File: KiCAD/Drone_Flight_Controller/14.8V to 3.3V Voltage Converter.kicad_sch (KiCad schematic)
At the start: 14 parts, among them Q1 BUJ303B,127, U4 AS358, U6 AS358

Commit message: Fix Bugs
Fix Bugs
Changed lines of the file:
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@@
-	)
-	(junction
-		(at 189.23 101.6)
-		(diameter 0)
-		(color 0 0 0 0)
 	)
 	(junction
@@
 	(wire
 		(pts
-			(xy 196.85 101.6) (xy 189.23 101.6)
-		)
-		(stroke
-			(width 0)
-			(type default)
-		)
-	)
-	(wire
-		(pts
 			(xy 162.56 90.17) (xy 165.1 90.17)
 		)
@@
 	(wire
 		(pts
-			(xy 114.3 111.76) (xy 87.63 111.76)
+			(xy 124.46 111.76) (xy 87.63 111.76)
 		)
 		(stroke
@@
 	(wire
 		(pts
-			(xy 114.3 90.17) (xy 114.3 111.76)
+			(xy 124.46 90.17) (xy 124.46 111.76)
 		)
 		(stroke
@@
 	(wire
 		(pts
-			(xy 196.85 99.06) (xy 196.85 101.6)
-		)
-		(stroke
-			(width 0)
-			(type default)
-		)
-	)
-	(wire
-		(pts
 			(xy 87.63 111.76) (xy 87.63 90.17)
 		)
@@
 	(wire
 		(pts
-			(xy 114.3 90.17) (xy 127 90.17)
+			(xy 124.46 90.17) (xy 127 90.17)
 		)
 		(stroke
@@
 			)
 		)
-		(property "Datasheet" "https://www.mouser.at/datasheet/2/115/DIOD_S_A0005046231_1-2542568.pdf"
+		(property "Datasheet" "~"
 			(at 154.94 90.17 0)
 			(effects
@@
 					(unit 1)
 				)
-			)
-		)
-	)
-	(symbol
-		(lib_id "power:PWR_FLAG")
-		(at 196.85 99.06 0)
-		(unit 1)
-		(exclude_from_sim no)
-		(in_bom yes)
-		(on_board yes)
-		(dnp no)
-		(fields_autoplaced yes)
-		(property "Reference" "#FLG01"
-			(at 196.85 97.155 0)
-			(effects
-				(font
-					(size 1.27 1.27)
-				)
-				(hide yes)
-			)
-		)
-		(property "Value" "PWR_FLAG"
-			(at 196.85 93.98 0)
-			(effects
-				(font
-					(size 1.27 1.27)
-				)
-			)
-		)
-		(property "Footprint" ""
-			(at 196.85 99.06 0)
-			(effects
-				(font
-					(size 1.27 1.27)
-				)
-				(hide yes)
-			)
-		)
-		(property "Datasheet" "~"
-			(at 196.85 99.06 0)
-			(effects
-				(font
-					(size 1.27 1.27)
-				)
-				(hide yes)
-			)
-		)
-		(property "Description" "Special symbol for telling ERC where power comes from"
-			(at 196.85 99.06 0)
-			(effects
-				(font
-					(size 1.27 1.27)
-				)
-				(hide yes)
-			)
-		)
-		(pin "1"
-		)
-		(instances
-			(project ""
-				(path "/05daaa24-e506-4b9a-9564-8bf799413ca8/93fa31b3-ffc2-4fc8-af5e-8c3024b36dbd"
-					(reference "#FLG01")
-					(unit 1)
-				)

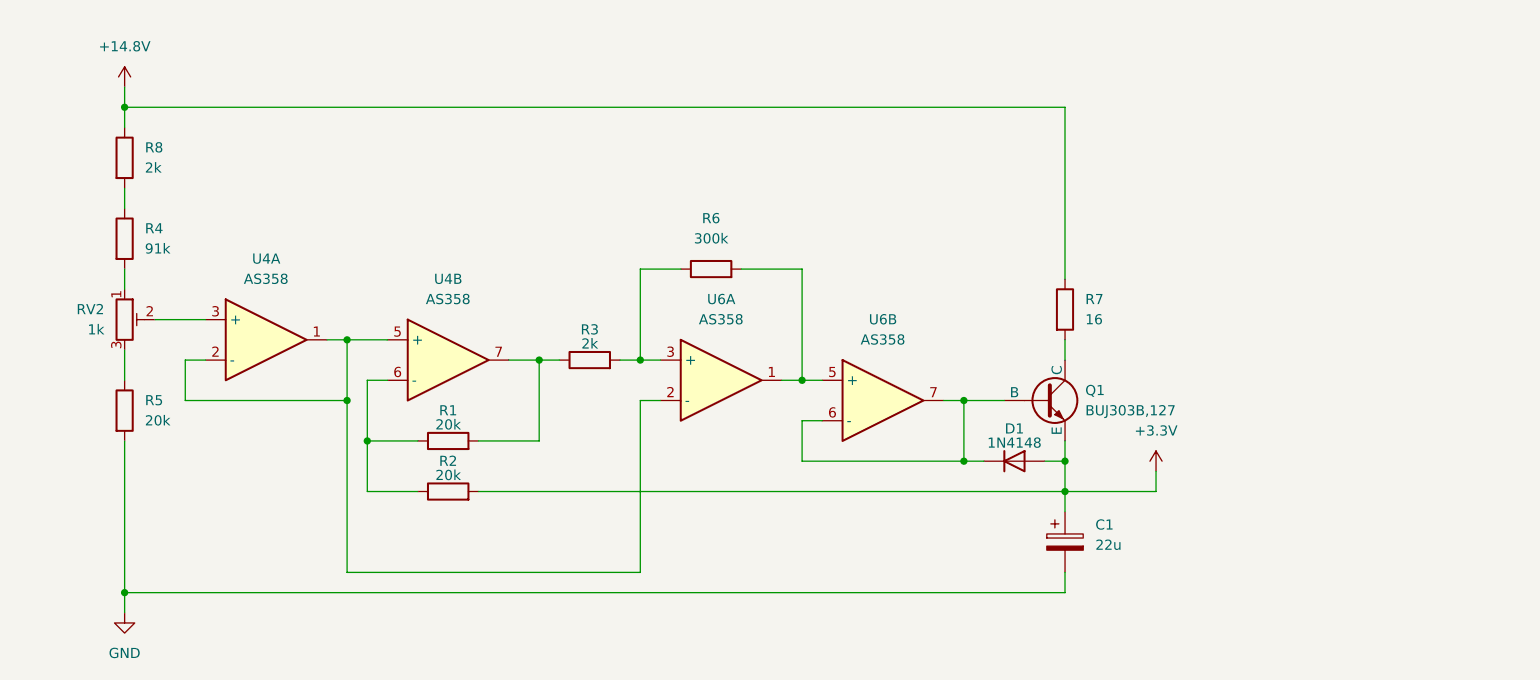
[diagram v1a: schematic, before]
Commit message: Change +14.8V & GND to +BATT & -BATT
Change +14.8V& GND to +BATT & -BATT
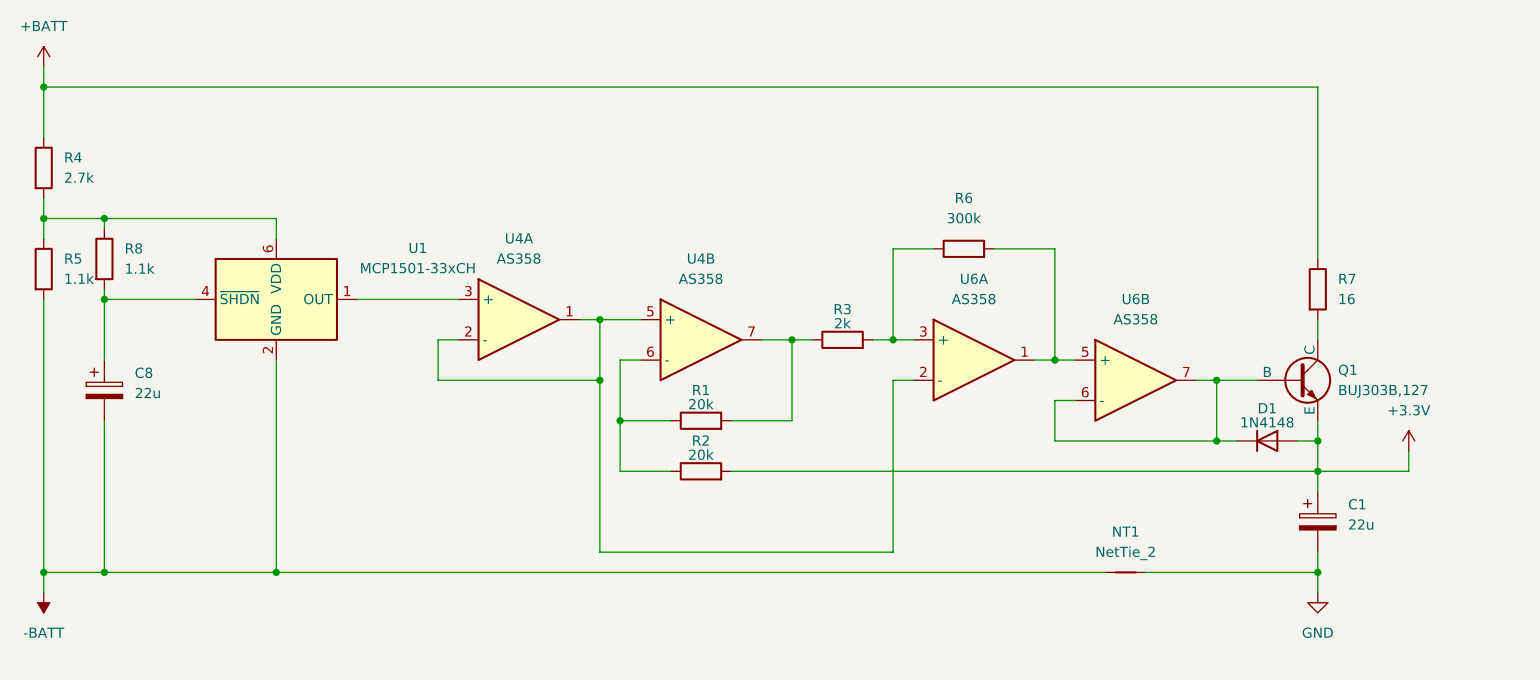
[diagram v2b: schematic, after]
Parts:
- removed RV2: 1k, Potentiometer_SMD:Potentiometer_Bourns_3214X_Vertical, symbol Device:R_Potentiometer_Trim
- added C8: 22u, Capacitor_THT:CP_Radial_D5.0mm_P2.00mm, symbol Device:C_Polarized
- added NT1: NetTie_2, symbol Device:NetTie_2
- added U1: MCP1501-33xCH, Package_TO_SOT_SMD:SOT-23-6, symbol Reference_Voltage:MCP1501-33xCH
- R4: value 91k -> 2.7k; footprint Resistor_SMD:R_0805_2012Metric_Pad1.20x1.40mm_HandSolder -> (none); Link https://www.mouser.at/ProductDetail/KOA-Speer/RN73R2ATTD750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 -> (none)
- R5: value 20k -> 1.1k; footprint Resistor_SMD:R_0805_2012Metric_Pad1.20x1.40mm_HandSolder -> (none); Link https://www.mouser.at/ProductDetail/Panasonic/ERA-6AEB203V?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 -> (none)
- R8: value 2k -> 1.1k; footprint Resistor_SMD:R_0805_2012Metric_Pad1.20x1.40mm_HandSolder -> (none); Link https://www.mouser.at/ProductDetail/YAGEO/RT0805BRD072KL?qs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 -> (none)
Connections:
- net GND: now also NT1.2; no longer R5.2
- net at R4.2: now also R5.1, R8.1, U1.6 (VDD)
- net at U4.3 (+): now also U1.1 (OUT)
- net at R8.2: now also C8.1, U1.4 (~{SHDN}); no longer R4.1
- net +14.8V renamed +BATT
- net +BATT: now also R4.1; no longer R8.1
- new net -BATT: C8.2, NT1.1, R5.2, U1.2 (GND), U1.3 (GND), U1.5 (GND)
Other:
- moved on the sheet: C1, D1, Q1, R1, R2, R3, R6, R7, U4A, U4B, U6A, U6B

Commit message: Add USB & Status LEDS
Add USB & Status LEDS
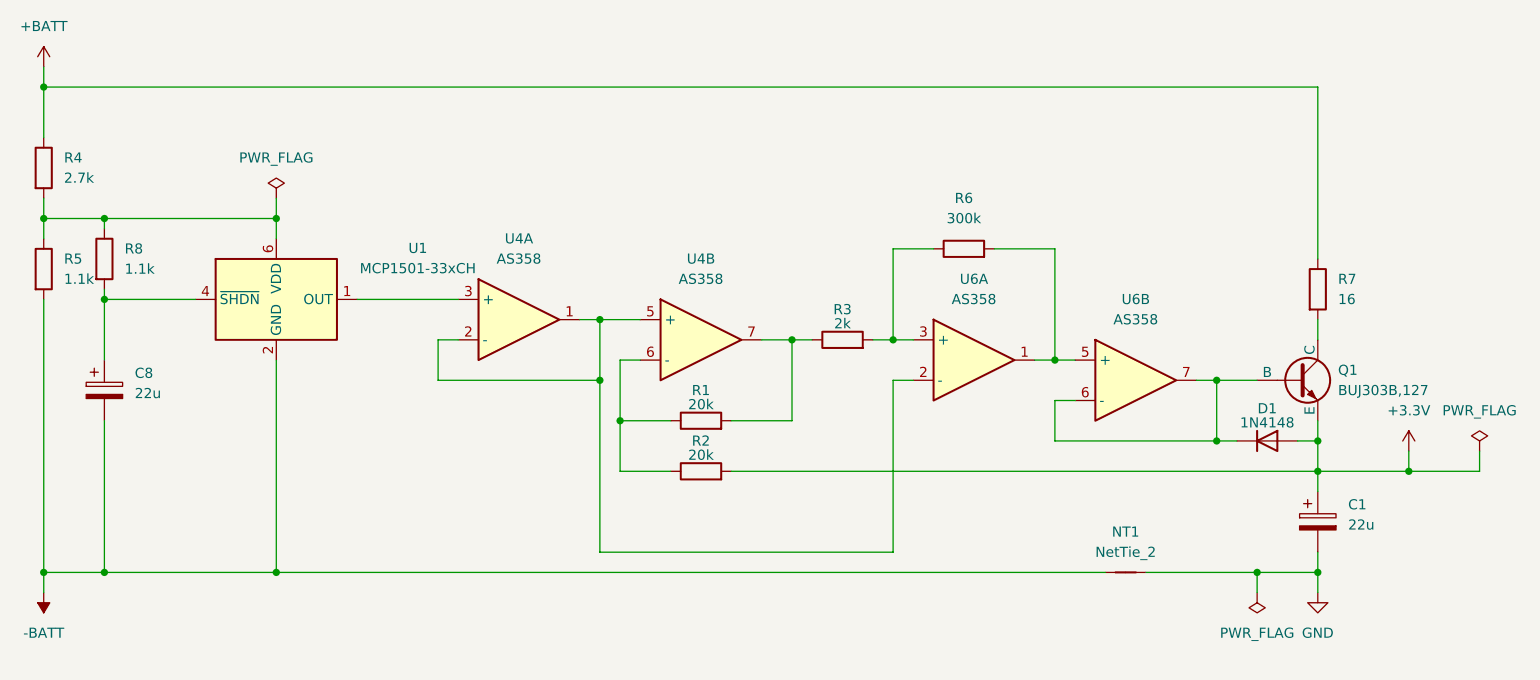
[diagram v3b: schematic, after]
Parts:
- NT1: Link (none) -> /
- R4: footprint (none) -> Resistor_SMD:R_0805_2012Metric_Pad1.20x1.40mm_HandSolder; Link (none) -> https://www.mouser.at/ProductDetail/Panasonic/ERA-6AEB272V?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
- R5, R8: footprint (none) -> Resistor_SMD:R_0805_2012Metric_Pad1.20x1.40mm_HandSolder; Link (none) -> https://www.mouser.at/ProductDetail/Panasonic/ERA-6AEB112V?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
- U1: Link (none) -> https://www.mouser.at/ProductDetail/Microchip-Technology/MC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

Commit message: Reanotate
Reanotate
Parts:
- renumbered C8 to C201, C1 to C202, D1 to D201, NT1 to NT201, Q1 to Q201, R4 to R201, R5 to R202, R8 to R203, R1 to R204, R2 to R205, R3 to R206, R6 to R207, R7 to R208, U1 to U201, U4 to U202, U6 to U203
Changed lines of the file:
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@@
 		(dnp no)
 		(fields_autoplaced yes)
-		(property "Reference" "R6"
+		(property "Reference" "R207"
 			(at 165.1 64.77 90)
 			(effects
@@
 			(project ""
 				(path "/05daaa24-e506-4b9a-9564-8bf799413ca8/93fa31b3-ffc2-4fc8-af5e-8c3024b36dbd"
-					(reference "R6")
+					(reference "R207")
 					(unit 1)
 				)
@@
 		(dnp no)
 		(fields_autoplaced yes)
-		(property "Reference" "#FLG07"
+		(property "Reference" "#FLG0203"
 			(at 229.87 94.615 0)
 			(effects
@@
 			(project ""
 				(path "/05daaa24-e506-4b9a-9564-8bf799413ca8/93fa31b3-ffc2-4fc8-af5e-8c3024b36dbd"
-					(reference "#FLG07")
+					(reference "#FLG0203")
 					(unit 1)
 				)
@@
 		(dnp no)
 		(fields_autoplaced yes)
-		(property "Reference" "C1"
+		(property "Reference" "C202"
 			(at 213.36 103.2509 0)
 			(effects
@@
 			(project ""
 				(path "/05daaa24-e506-4b9a-9564-8bf799413ca8/93fa31b3-ffc2-4fc8-af5e-8c3024b36dbd"
-					(reference "C1")
+					(reference "C202")
 					(unit 1)
 				)
@@
 		(dnp no)
 		(fields_autoplaced yes)
-		(property "Reference" "#PWR04"
+		(property "Reference" "#PWR0202"
 			(at 49.53 110.49 0)
 			(effects
@@
 			(project ""
 				(path "/05daaa24-e506-4b9a-9564-8bf799413ca8/93fa31b3-ffc2-4fc8-af5e-8c3024b36dbd"
-					(reference "#PWR04")
+					(reference "#PWR0202")
 					(unit 1)
 				)
@@
 		(on_board yes)
 		(dnp no)
-		(property "Reference" "R2"
+		(property "Reference" "R205"
 			(at 132.08 95.25 90)
 			(effects
@@
 			(project "Drone_Flight_Controller"
 				(path "/05daaa24-e506-4b9a-9564-8bf799413ca8/93fa31b3-ffc2-4fc8-af5e-8c3024b36dbd"
-					(reference "R2")
+					(reference "R205")
 					(unit 1)
 				)
@@
 		(dnp no)
 		(fields_autoplaced yes)
-		(property "Reference" "R8"
+		(property "Reference" "R203"
 			(at 59.69 71.1199 0)
 			(effects
@@
 			(project ""
 				(path "/05daaa24-e506-4b9a-9564-8bf799413ca8/93fa31b3-ffc2-4fc8-af5e-8c3024b36dbd"
-					(reference "R8")
+					(reference "R203")
 					(unit 1)
 				)
@@
 		(dnp no)
 		(fields_autoplaced yes)
-		(property "Reference" "#PWR02"
+		(property "Reference" "#PWR0201"
 			(at 49.53 52.07 0)
 			(effects
@@
 			(project ""
 				(path "/05daaa24-e506-4b9a-9564-8bf799413ca8/93fa31b3-ffc2-4fc8-af5e-8c3024b36dbd"
-					(reference "#PWR02")
+					(reference "#PWR0201")
 					(unit 1)
 				)
@@
 		(dnp no)
 		(fields_autoplaced yes)
-		(property "Reference" "R7"
+		(property "Reference" "R208"
 			(at 212.09 74.9299 0)
 			(effects
@@
 			(project ""
 				(path "/05daaa24-e506-4b9a-9564-8bf799413ca8/93fa31b3-ffc2-4fc8-af5e-8c3024b36dbd"
-					(reference "R7")
+					(reference "R208")
 					(unit 1)
 				)
@@
 		(dnp no)
 		(fields_autoplaced yes)
-		(property "Reference" "U6"
+		(property "Reference" "U203"
 			(at 186.69 77.47 0)
 			(effects
@@
 			(project ""
 				(path "/05daaa24-e506-4b9a-9564-8bf799413ca8/93fa31b3-ffc2-4fc8-af5e-8c3024b36dbd"
-					(reference "U6")
+					(reference "U203")
 					(unit 2)
 				)
@@
 		(dnp no)
 		(fields_autoplaced yes)
-		(property "Reference" "#PWR017"
+		(property "Reference" "#PWR0203"
 			(at 209.55 120.65 0)
 			(effects
@@
 			(project ""
 				(path "/05daaa24-e506-4b9a-9564-8bf799413ca8/93fa31b3-ffc2-4fc8-af5e-8c3024b36dbd"
-					(reference "#PWR017")
+					(reference "#PWR0203")
 					(unit 1)
 				)
@@
 		(dnp no)
 		(fields_autoplaced yes)
-		(property "Reference" "R5"
+		(property "Reference" "R202"
 			(at 52.07 72.3899 0)
 			(effects
@@
 			(project "Drone_Flight_Controller"
 				(path "/05daaa24-e506-4b9a-9564-8bf799413ca8/93fa31b3-ffc2-4fc8-af5e-8c3024b36dbd"
-					(reference "R5")
+					(reference "R202")
 					(unit 1)
 				)
@@
 		(dnp no)
 		(fields_autoplaced yes)
-		(property "Reference" "NT1"
+		(property "Reference" "NT201"
 			(at 185.42 106.68 0)
 			(effects
@@
 			(project ""
 				(path "/05daaa24-e506-4b9a-9564-8bf799413ca8/93fa31b3-ffc2-4fc8-af5e-8c3024b36dbd"
-					(reference "NT1")
+					(reference "NT201")
 					(unit 1)
 				)
@@
 		(dnp no)
 		(fields_autoplaced yes)
-		(property "Reference" "U4"
+		(property "Reference" "U202"
 			(at 132.08 72.39 0)
 			(effects
@@
 			(project "Drone_Flight_Controller"
 				(path "/05daaa24-e506-4b9a-9564-8bf799413ca8/93fa31b3-ffc2-4fc8-af5e-8c3024b36dbd"
-					(reference "U4")
+					(reference "U202")
 					(unit 2)
 				)
@@
 		(on_board yes)
 		(dnp no)
-		(property "Reference" "R3"
+		(property "Reference" "R206"
 			(at 149.86 78.74 90)
 			(effects
@@
 			(project "Drone_Flight_Controller"
 				(path "/05daaa24-e506-4b9a-9564-8bf799413ca8/93fa31b3-ffc2-4fc8-af5e-8c3024b36dbd"
-					(reference "R3")
+					(reference "R206")
 					(unit 1)
 				)
@@
 		(dnp no)
 		(fields_autoplaced yes)
-		(property "Reference" "U4"
+		(property "Reference" "U202"
 			(at 109.22 69.85 0)
 			(effects
@@
 			(project "Drone_Flight_Controller"
 				(path "/05daaa24-e506-4b9a-9564-8bf799413ca8/93fa31b3-ffc2-4fc8-af5e-8c3024b36dbd"
-					(reference "U4")
+					(reference "U202")
 					(unit 1)
 				)
@@
 		(dnp no)
 		(fields_autoplaced yes)
-		(property "Reference" "R4"
+		(property "Reference" "R201"
 			(at 52.07 59.6899 0)
 			(effects
@@
 			(project ""
 				(path "/05daaa24-e506-4b9a-9564-8bf799413ca8/93fa31b3-ffc2-4fc8-af5e-8c3024b36dbd"
-					(reference "R4")
+					(reference "R201")
 					(unit 1)
 				)
@@
 		(on_board yes)
 		(dnp no)
-		(property "Reference" "D1"
+		(property "Reference" "D201"
 			(at 203.2 91.186 0)
 			(effects
@@
 			(project ""
 				(path "/05daaa24-e506-4b9a-9564-8bf799413ca8/93fa31b3-ffc2-4fc8-af5e-8c3024b36dbd"
-					(reference "D1")
+					(reference "D201")
 					(unit 1)
 				)
@@
 		(dnp no)
 		(fields_autoplaced yes)
-		(property "Reference" "#FLG01"
+		(property "Reference" "#FLG0202"
 			(at 201.93 116.205 0)
 			(effects
@@
 			(project ""
 				(path "/05daaa24-e506-4b9a-9564-8bf799413ca8/93fa31b3-ffc2-4fc8-af5e-8c3024b36dbd"
-					(reference "#FLG01")
+					(reference "#FLG0202")
 					(unit 1)
 				)
@@
 		(on_board yes)
 		(dnp no)
-		(property "Reference" "R1"
+		(property "Reference" "R204"
 			(at 132.08 88.9 90)
 			(effects
@@
 			(project ""
 				(path "/05daaa24-e506-4b9a-9564-8bf799413ca8/93fa31b3-ffc2-4fc8-af5e-8c3024b36dbd"
-					(reference "R1")
+					(reference "R204")
 					(unit 1)
 				)
@@
 		(dnp no)
 		(fields_autoplaced yes)
-		(property "Reference" "U6"
+		(property "Reference" "U203"
 			(at 166.37 74.93 0)
 			(effects
@@
 			(project ""
 				(path "/05daaa24-e506-4b9a-9564-8bf799413ca8/93fa31b3-ffc2-4fc8-af5e-8c3024b36dbd"
-					(reference "U6")
+					(reference "U203")
 					(unit 1)
 				)
@@
 		(dnp no)
 		(fields_autoplaced yes)
-		(property "Reference" "#FLG05"
+		(property "Reference" "#FLG0201"
 			(at 78.74 62.865 0)
 			(effects
@@
 			(project ""
 				(path "/05daaa24-e506-4b9a-9564-8bf799413ca8/93fa31b3-ffc2-4fc8-af5e-8c3024b36dbd"
-					(reference "#FLG05")
+					(reference "#FLG0201")
 					(unit 1)
 				)
@@
 		(dnp no)
 		(fields_autoplaced yes)
-		(property "Reference" "C8"
+		(property "Reference" "C201"
 			(at 60.96 86.7409 0)
 			(effects
@@
 			(project "Drone_Flight_Controller"
 				(path "/05daaa24-e506-4b9a-9564-8bf799413ca8/93fa31b3-ffc2-4fc8-af5e-8c3024b36dbd"
-					(reference "C8")
+					(reference "C201")
 					(unit 1)
 				)
@@
 		(dnp no)
 		(fields_autoplaced yes)
-		(property "Reference" "#PWR03"
+		(property "Reference" "#PWR0204"
 			(at 220.98 100.33 0)
 			(effects
@@
 			(project ""
 				(path "/05daaa24-e506-4b9a-9564-8bf799413ca8/93fa31b3-ffc2-4fc8-af5e-8c3024b36dbd"
-					(reference "#PWR03")
+					(reference "#PWR0204")
 					(unit 1)
 				)
@@
 		(dnp no)
 		(fields_autoplaced yes)
-		(property "Reference" "U1"
+		(property "Reference" "U201"
 			(at 96.52 71.0498 0)
 			(effects
@@
 			(project ""
 				(path "/05daaa24-e506-4b9a-9564-8bf799413ca8/93fa31b3-ffc2-4fc8-af5e-8c3024b36dbd"
-					(reference "U1")
+					(reference "U201")
 					(unit 1)
 				)
@@
 		(dnp no)
 		(fields_autoplaced yes)
-		(property "Reference" "Q1"
+		(property "Reference" "Q201"
 			(at 212.09 86.3599 0)
 			(effects
@@
 			(project ""
 				(path "/05daaa24-e506-4b9a-9564-8bf799413ca8/93fa31b3-ffc2-4fc8-af5e-8c3024b36dbd"
-					(reference "Q1")
-					(unit 1)
-				)
+					(reference "Q201")
+					(unit 1)
+				)

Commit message: Reannotate
Reannotate
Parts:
- renumbered R207 to R202, R202 to R204, R208 to R205, R204 to R207, R205 to R208
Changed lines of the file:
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@@
 		(dnp no)
 		(fields_autoplaced yes)
-		(property "Reference" "R207"
+		(property "Reference" "R202"
 			(at 165.1 64.77 90)
 			(effects
@@
 			(project ""
 				(path "/05daaa24-e506-4b9a-9564-8bf799413ca8/93fa31b3-ffc2-4fc8-af5e-8c3024b36dbd"
-					(reference "R207")
+					(reference "R202")
 					(unit 1)
 				)
@@
 		(dnp no)
 		(fields_autoplaced yes)
-		(property "Reference" "#FLG0203"
+		(property "Reference" "#FLG0202"
 			(at 229.87 94.615 0)
 			(effects
@@
 			(project ""
 				(path "/05daaa24-e506-4b9a-9564-8bf799413ca8/93fa31b3-ffc2-4fc8-af5e-8c3024b36dbd"
-					(reference "#FLG0203")
+					(reference "#FLG0202")
 					(unit 1)
 				)
@@
 		(dnp no)
 		(fields_autoplaced yes)
-		(property "Reference" "#PWR0202"
+		(property "Reference" "#PWR0203"
 			(at 49.53 110.49 0)
 			(effects
@@
 			(project ""
 				(path "/05daaa24-e506-4b9a-9564-8bf799413ca8/93fa31b3-ffc2-4fc8-af5e-8c3024b36dbd"
-					(reference "#PWR0202")
+					(reference "#PWR0203")
 					(unit 1)
 				)
@@
 		(on_board yes)
 		(dnp no)
-		(property "Reference" "R205"
+		(property "Reference" "R208"
 			(at 132.08 95.25 90)
 			(effects
@@
 			(project "Drone_Flight_Controller"
 				(path "/05daaa24-e506-4b9a-9564-8bf799413ca8/93fa31b3-ffc2-4fc8-af5e-8c3024b36dbd"
-					(reference "R205")
+					(reference "R208")
 					(unit 1)
 				)
@@
 		(dnp no)
 		(fields_autoplaced yes)
-		(property "Reference" "R208"
+		(property "Reference" "R205"
 			(at 212.09 74.9299 0)
 			(effects
@@
 			(project ""
 				(path "/05daaa24-e506-4b9a-9564-8bf799413ca8/93fa31b3-ffc2-4fc8-af5e-8c3024b36dbd"
-					(reference "R208")
+					(reference "R205")
 					(unit 1)
 				)
@@
 		(dnp no)
 		(fields_autoplaced yes)
-		(property "Reference" "#PWR0203"
+		(property "Reference" "#PWR0204"
 			(at 209.55 120.65 0)
 			(effects
@@
 			(project ""
 				(path "/05daaa24-e506-4b9a-9564-8bf799413ca8/93fa31b3-ffc2-4fc8-af5e-8c3024b36dbd"
-					(reference "#PWR0203")
+					(reference "#PWR0204")
 					(unit 1)
 				)
@@
 		(dnp no)
 		(fields_autoplaced yes)
-		(property "Reference" "R202"
+		(property "Reference" "R204"
 			(at 52.07 72.3899 0)
 			(effects
@@
 			(project "Drone_Flight_Controller"
 				(path "/05daaa24-e506-4b9a-9564-8bf799413ca8/93fa31b3-ffc2-4fc8-af5e-8c3024b36dbd"
-					(reference "R202")
+					(reference "R204")
 					(unit 1)
 				)
@@
 		(dnp no)
 		(fields_autoplaced yes)
-		(property "Reference" "#FLG0202"
+		(property "Reference" "#FLG0203"
 			(at 201.93 116.205 0)
 			(effects
@@
 			(project ""
 				(path "/05daaa24-e506-4b9a-9564-8bf799413ca8/93fa31b3-ffc2-4fc8-af5e-8c3024b36dbd"
-					(reference "#FLG0202")
+					(reference "#FLG0203")
 					(unit 1)
 				)
@@
 		(on_board yes)
 		(dnp no)
-		(property "Reference" "R204"
+		(property "Reference" "R207"
 			(at 132.08 88.9 90)
 			(effects
@@
 			(project ""
 				(path "/05daaa24-e506-4b9a-9564-8bf799413ca8/93fa31b3-ffc2-4fc8-af5e-8c3024b36dbd"
-					(reference "R204")
+					(reference "R207")
 					(unit 1)
 				)
@@
 		(dnp no)
 		(fields_autoplaced yes)
-		(property "Reference" "#PWR0204"
+		(property "Reference" "#PWR0202"
 			(at 220.98 100.33 0)
 			(effects
@@
 			(project ""
 				(path "/05daaa24-e506-4b9a-9564-8bf799413ca8/93fa31b3-ffc2-4fc8-af5e-8c3024b36dbd"
-					(reference "#PWR0204")
-					(unit 1)
-				)
+					(reference "#PWR0202")
+					(unit 1)
+				)

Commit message: Add Footprint to NetTie
Add Footprint to NetTie
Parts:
- NT201: footprint (none) -> NetTie:NetTie-2_SMD_Pad2.0mm
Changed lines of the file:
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@@
 			)
 		)
-		(property "Footprint" ""
+		(property "Footprint" "NetTie:NetTie-2_SMD_Pad2.0mm"
 			(at 185.42 111.76 0)
 			(effects
